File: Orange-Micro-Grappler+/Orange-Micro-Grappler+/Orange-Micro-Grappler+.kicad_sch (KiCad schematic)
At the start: 24 parts, among them J1 Conn_02x13, J2 AppleIIBus, Q1 2N3904, U1 74LS00, U10 74LS373, U11 74LS373, U2 74LS279, U3 74LS02, U4 74LS00, U5 74LS74, U6 74LS00, U7 74LS08, U8 74LS30, U9 27C32

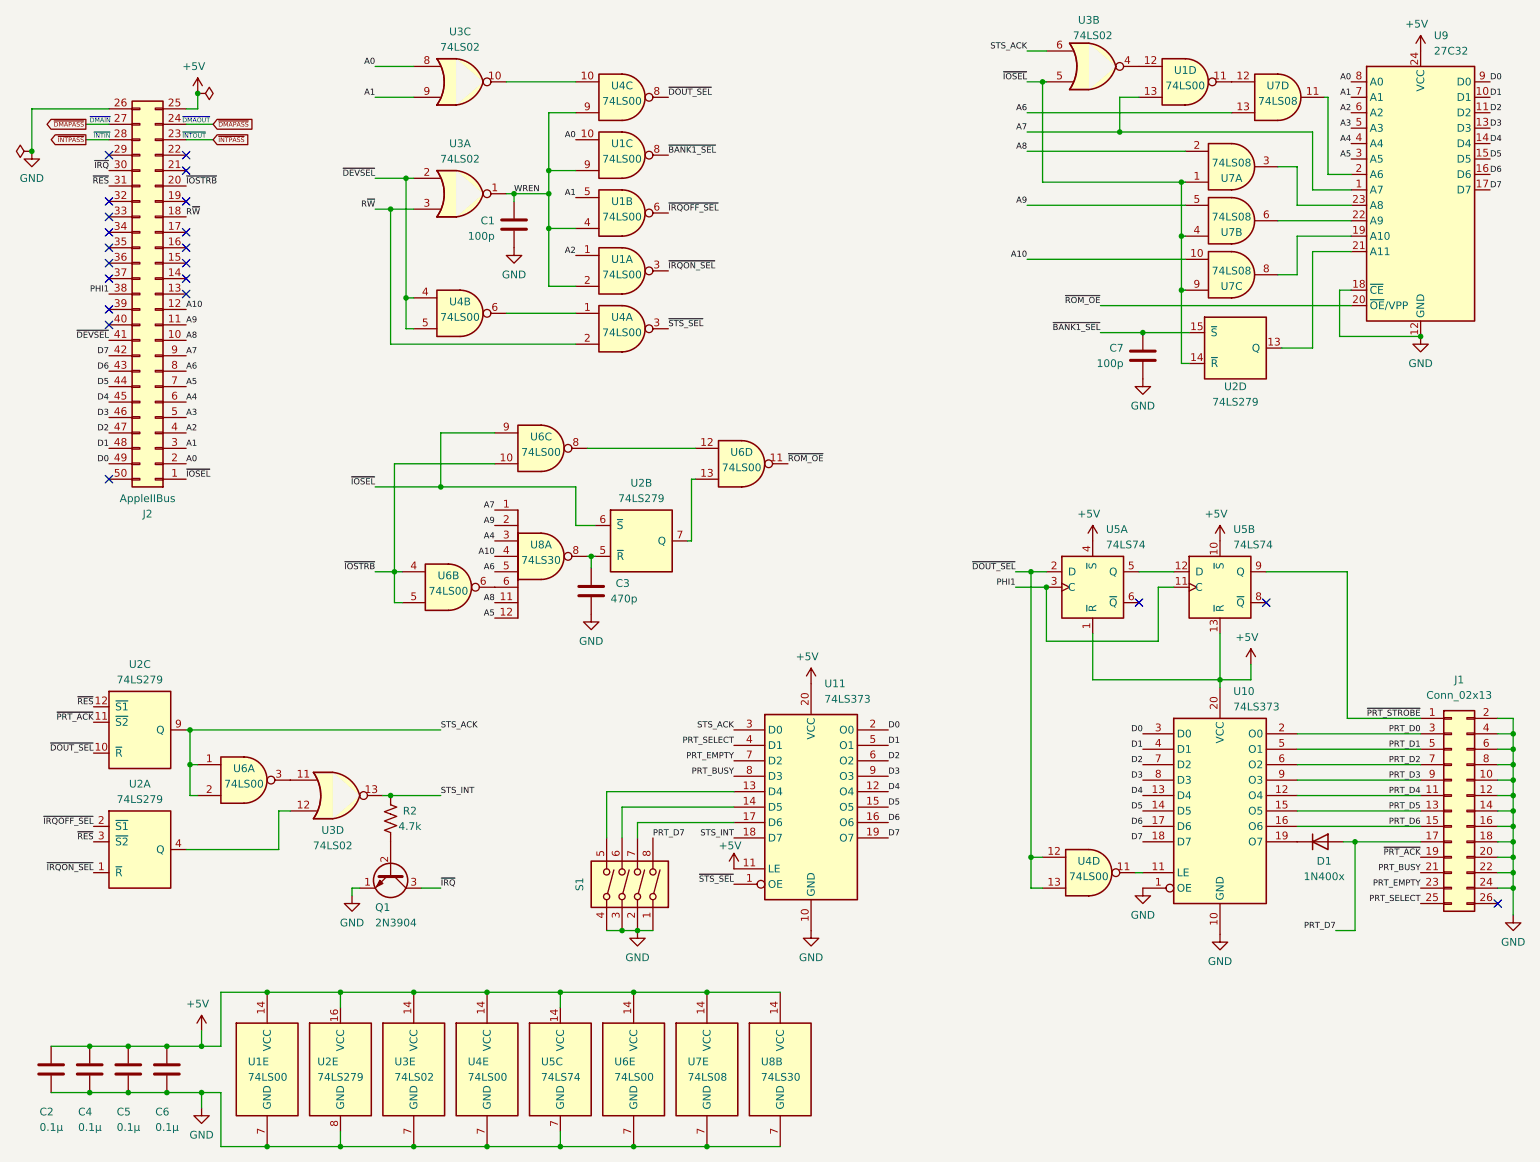
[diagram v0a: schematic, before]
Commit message: Update Grappler projects to kicad8 and the shared symbol library
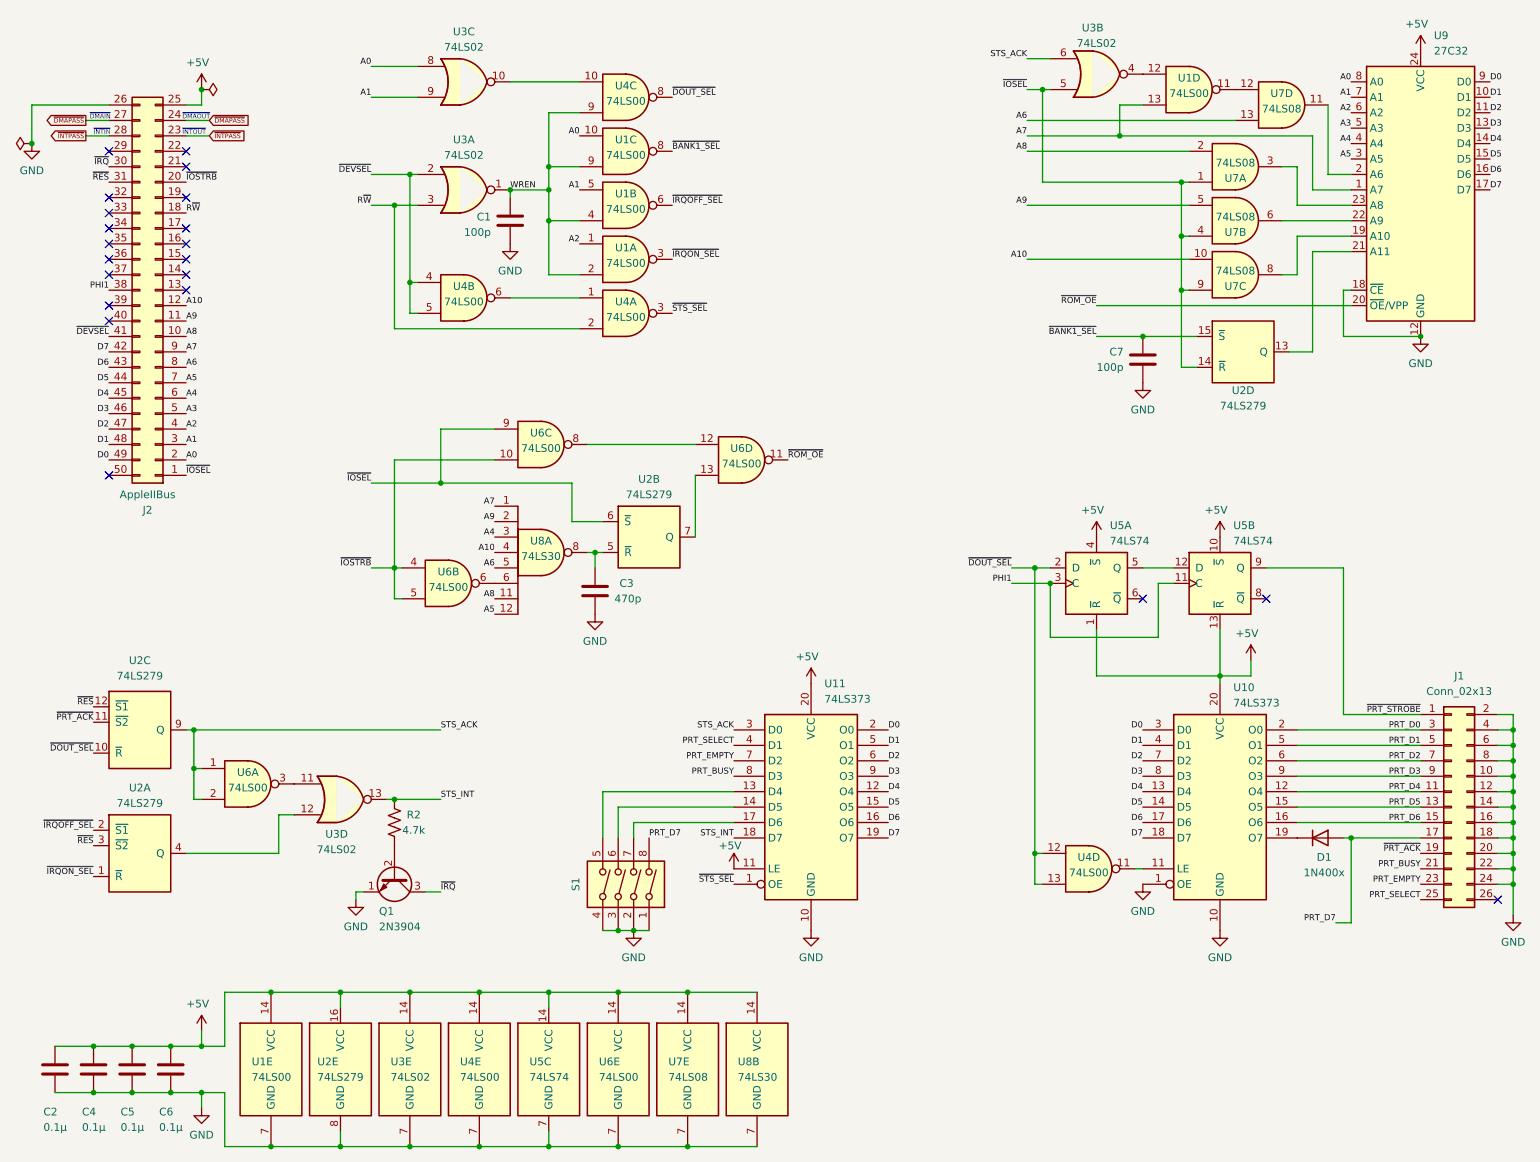
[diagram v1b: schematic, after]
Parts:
- U2: symbol Logic:74LS279 -> Logic_Legacy:74LS279
- U9: symbol Memory:27C32 -> Memory_Legacy:27C32
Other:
- moved on the sheet: C1, C2, C3, C4, C5, C6, C7, D1, J1, J2, Q1, R2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
